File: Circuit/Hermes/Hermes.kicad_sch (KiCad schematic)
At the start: 3 parts, among them U1 VL53L0CXV0DH1, U2 XIAO-RP2040-DIP

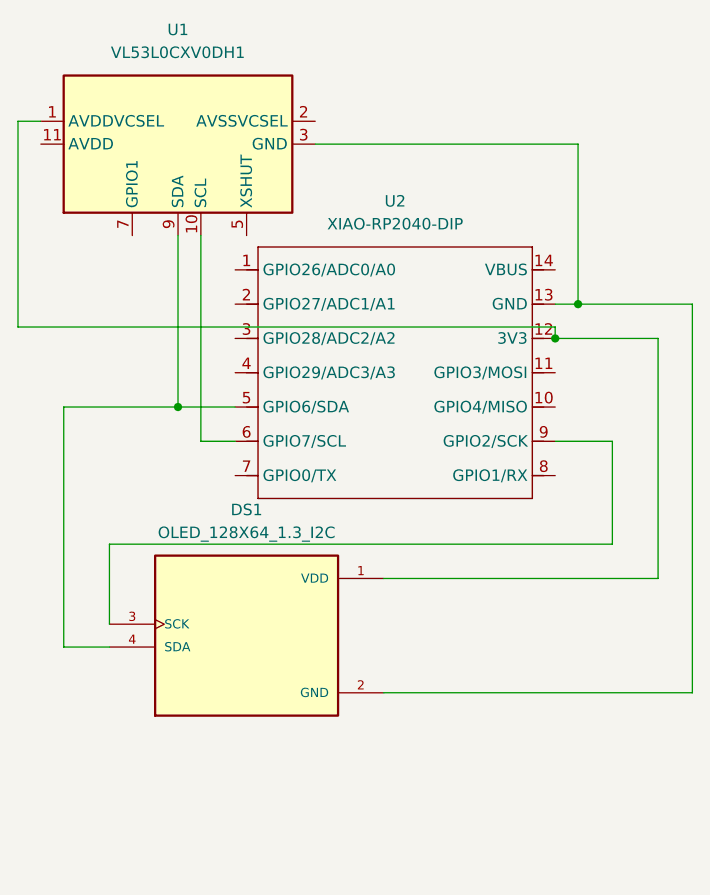
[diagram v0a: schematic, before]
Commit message: Add new components and update code for temperature and distance measurement
- Updated fp-lib-table and sym-lib-table to include new libraries: LM393, DHT11, BUTT-2, HC-SR04, and ARDUINO_NANO.
- Added LM393 component files including symbol and footprint.
- Created a redirection HTML file for LM393 import instructions.
- Modified the Arduino code to integrate DHT11 sensor for temperature and humidity readings.
- Implemented button functionality to toggle between temperature and distance display modes.
- Updated display logic to show sensor data based on the selected mode.
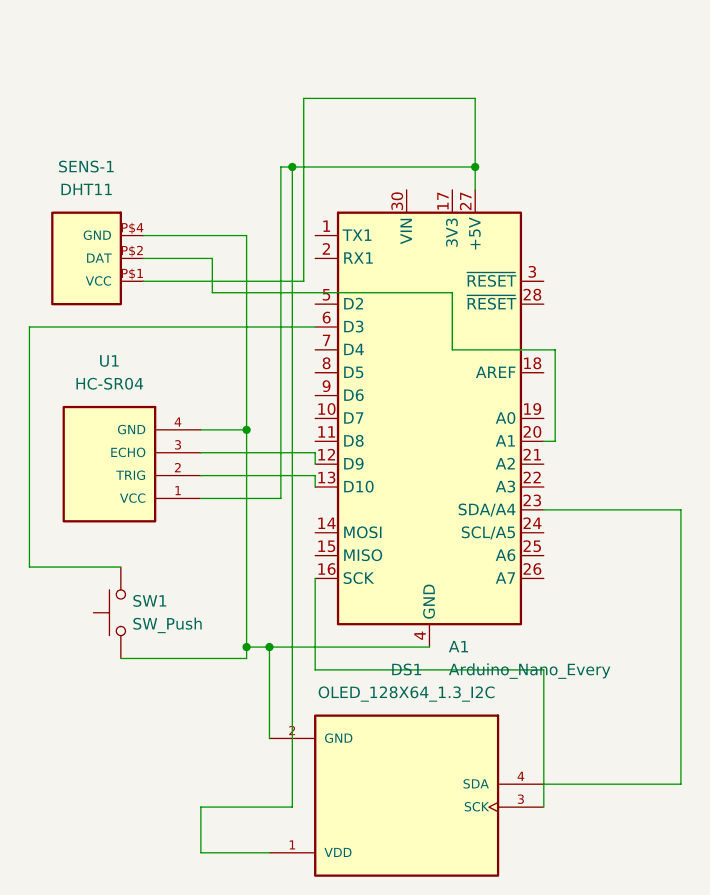
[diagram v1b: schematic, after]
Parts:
- removed U1: VL53L0CXV0DH1, Sensor_Distance:ST_VL53L1x, symbol Sensor_Distance:VL53L0CXV0DH1
- removed U2: XIAO-RP2040-DIP, OPL_Kicad:XIAO-RP2040-DIP, symbol Seeed_Studio_XIAO_Series:XIAO-RP2040-DIP
- added A1: Arduino_Nano_Every, Module:Arduino_Nano, symbol MCU_Module:Arduino_Nano_Every
- added SENS-1: DHT11, DHT11:SENSOR-DHT11, symbol DHT11:DHT11
- added SW1: SW_Push, BUTT-2:SW_BUTT-2, symbol Switch:SW_Push
- added U1: HC-SR04, HC-SR04:XCVR_HC-SR04, symbol HC-SR04:HC-SR04
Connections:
- net at DS1.1 (VDD): now also A1.27 (+5V), SENS-1.P$1 (VCC), U1.1 (VCC)
- net at DS1.2 (GND): now also A1.29 (GND), A1.4 (GND), SENS-1.P$4 (GND), SW1.1, U1.4 (GND)
- net at DS1.4 (SDA): now also A1.23 (SDA/A4)
- net at DS1.3 (SCK): now also A1.16 (SCK)
- new net: A1.6 (D3), SW1.2
- new net: A1.13 (D10), U1.2 (TRIG)
- new net: A1.12 (D9), U1.3 (ECHO)
- new net: A1.20 (A1), SENS-1.P$2 (DAT)
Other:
- moved on the sheet: DS1

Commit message: Add new Gerber files for Hermes project and update job configuration
- Created new Gerber files: Hermes-F_Mask.gbr, Hermes-F_Paste.gbr, Hermes-F_Silkscreen.gbr
- Updated Hermes job configuration file (Hermes-job.gbrjob) with new file paths and specifications
- Removed outdated backup zip file (Hermes-2026-06-10_174330.zip) and added a new backup (Hermes-2026-06-10_213705.zip)
- Adjusted PCB settings in Hermes.kicad_pcb for output directory and drill shape
- Updated project properties in Hermes.kicad_pro to reflect new plot directory
- Made minor adjustments to schematic (Hermes.kicad_sch) for wire connections
- Refactored Arduino code in hermes_code.ino for better pin management and distance measurement logic
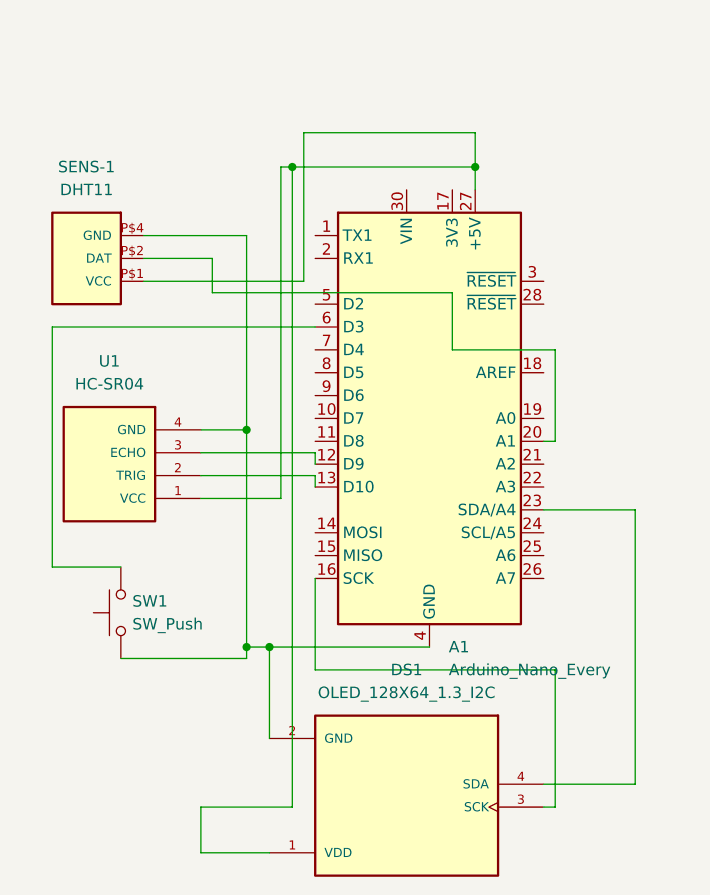
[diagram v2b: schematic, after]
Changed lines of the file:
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@@
 	(wire
 		(pts
-			(xy 191.77 54.61) (xy 191.77 62.23)
+			(xy 191.77 58.42) (xy 191.77 62.23)
 		)
 		(stroke
@@
 	(wire
 		(pts
-			(xy 199.39 130.81) (xy 214.63 130.81)
+			(xy 199.39 130.81) (xy 209.55 130.81)
 		)
 		(stroke
@@
 	(wire
 		(pts
-			(xy 142.24 106.68) (xy 142.24 80.01)
-		)
-		(stroke
-			(width 0)
-			(type default)
-		)
-	)
-	(wire
-		(pts
-			(xy 172.72 74.93) (xy 172.72 54.61)
+			(xy 144.78 106.68) (xy 144.78 80.01)
+		)
+		(stroke
+			(width 0)
+			(type default)
+		)
+	)
+	(wire
+		(pts
+			(xy 172.72 74.93) (xy 172.72 58.42)
 		)
 		(stroke
@@
 	(wire
 		(pts
-			(xy 152.4 106.68) (xy 142.24 106.68)
-		)
-		(stroke
-			(width 0)
-			(type default)
-		)
-	)
-	(wire
-		(pts
-			(xy 214.63 130.81) (xy 214.63 100.33)
+			(xy 152.4 106.68) (xy 144.78 106.68)
+		)
+		(stroke
+			(width 0)
+			(type default)
+		)
+	)
+	(wire
+		(pts
+			(xy 209.55 130.81) (xy 209.55 100.33)
+		)
+		(stroke
+			(width 0)
+			(type default)
+		)
+	)
+	(wire
+		(pts
+			(xy 200.66 133.35) (xy 199.39 133.35)
 		)
 		(stroke
@@
 	(wire
 		(pts
-			(xy 199.39 118.11) (xy 199.39 133.35)
+			(xy 200.66 118.11) (xy 200.66 133.35)
 		)
 		(stroke
@@
 	(wire
 		(pts
-			(xy 199.39 118.11) (xy 173.99 118.11)
-		)
-		(stroke
-			(width 0)
-			(type default)
-		)
-	)
-	(wire
-		(pts
-			(xy 172.72 54.61) (xy 191.77 54.61)
+			(xy 200.66 118.11) (xy 173.99 118.11)
+		)
+		(stroke
+			(width 0)
+			(type default)
+		)
+	)
+	(wire
+		(pts
+			(xy 172.72 58.42) (xy 191.77 58.42)
 		)
 		(stroke
@@
 	(wire
 		(pts
-			(xy 142.24 80.01) (xy 173.99 80.01)
+			(xy 144.78 80.01) (xy 173.99 80.01)
 		)
 		(stroke
@@
 	(wire
 		(pts
-			(xy 214.63 100.33) (xy 199.39 100.33)
-		)
-		(stroke
+			(xy 209.55 100.33) (xy 199.39 100.33)
+		)
+		(stroke
